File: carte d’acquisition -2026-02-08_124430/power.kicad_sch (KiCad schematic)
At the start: 59 parts, among them IC2 TPS259573DSGR, J10 Screw_Terminal_2_P5.00mm, U15 OKI-78SR-5_1.5-W36-C, U3 TPS55285, U4 MCP1799x-500xxTT, U5 INA3221, U9 TPS2116DRL

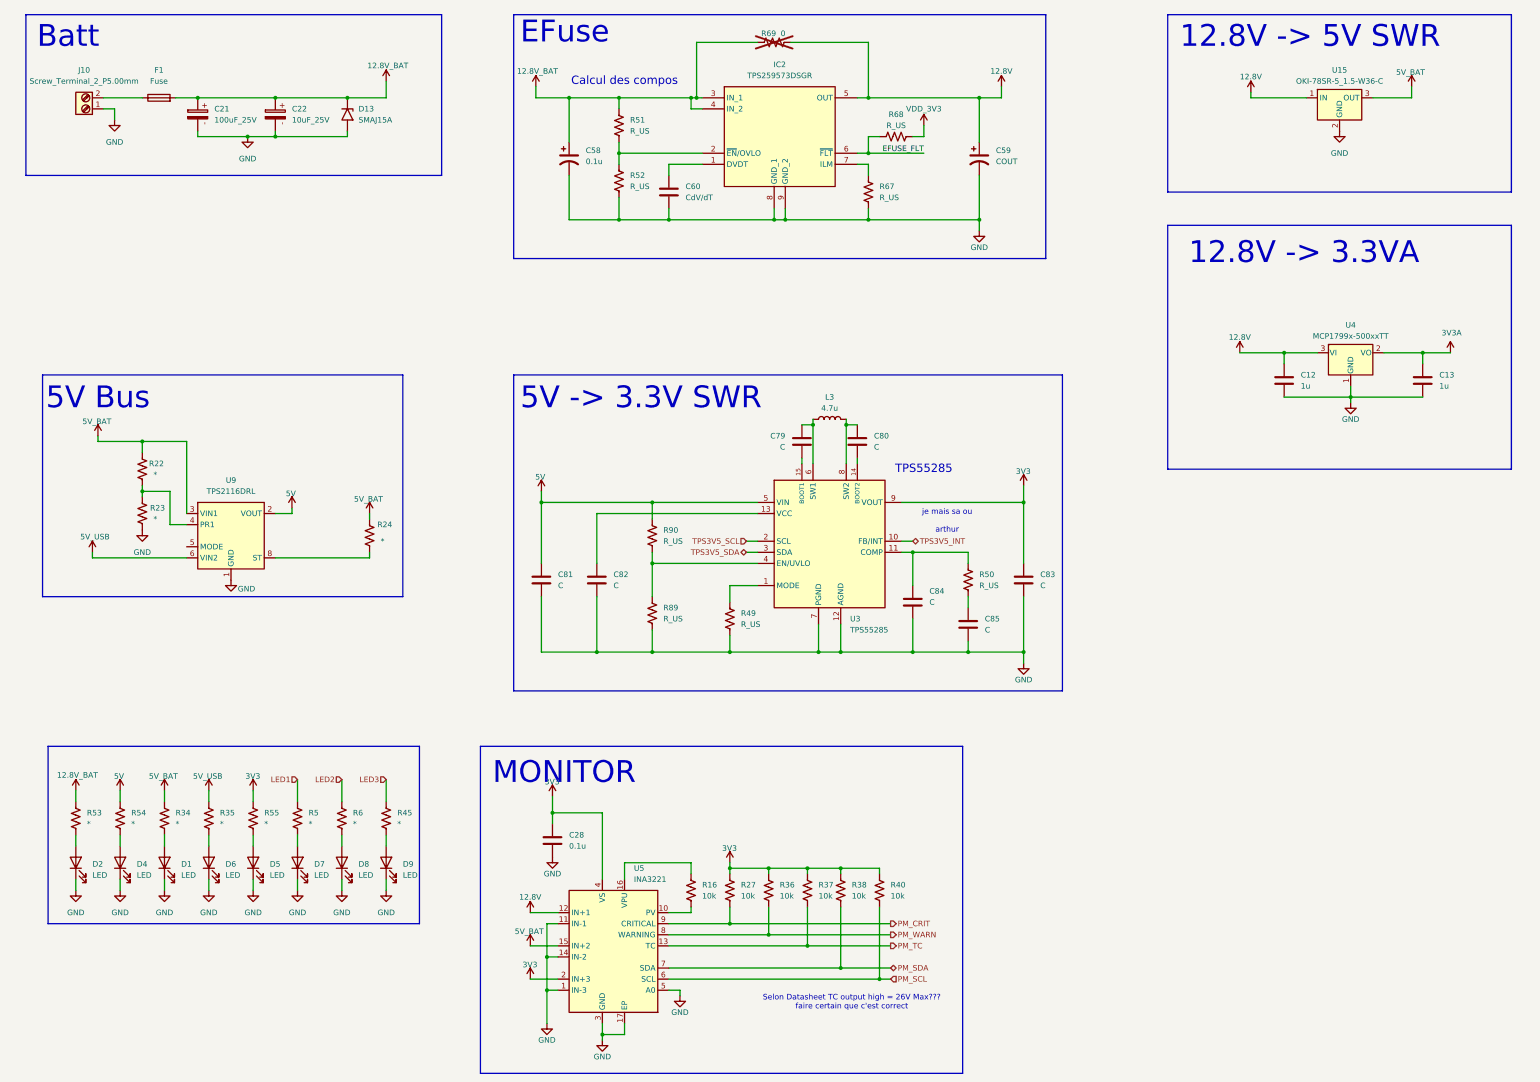
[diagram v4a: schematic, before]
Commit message: Ajout du 5VA et des borniers a vis pour loadcell
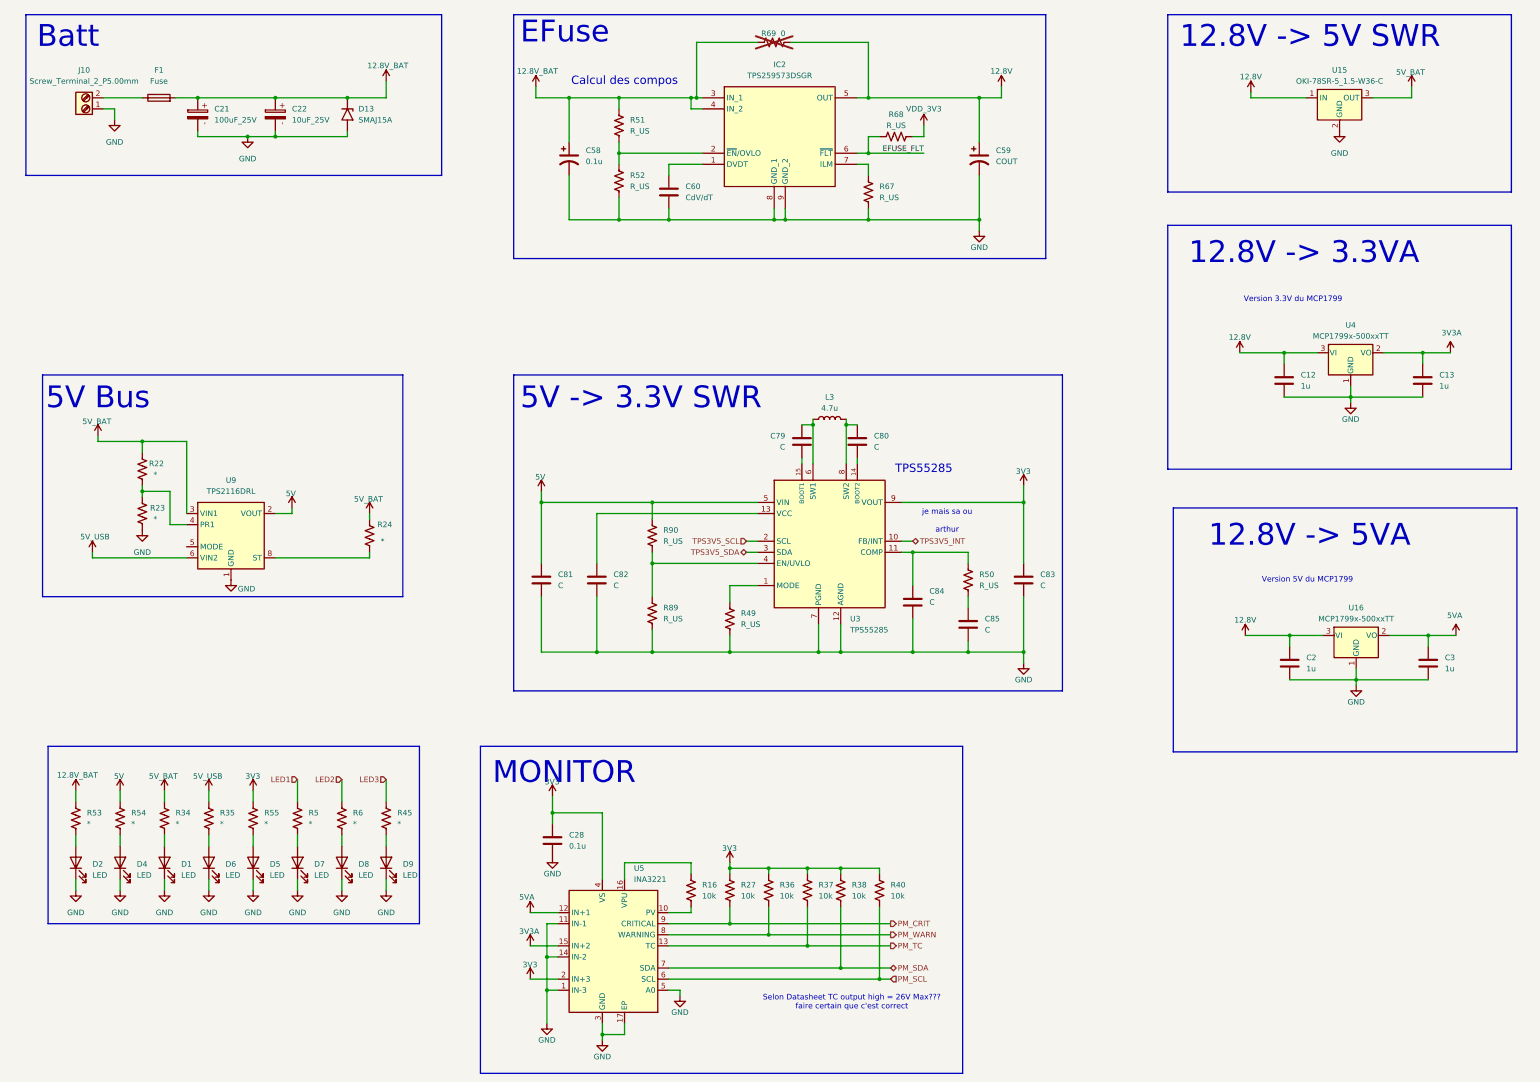
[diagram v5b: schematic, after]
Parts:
- added C2, C3: 1u, Capacitor_SMD:C_0603_1608Metric, symbol Device:C
- added U16: MCP1799x-500xxTT, Package_TO_SOT_SMD:SOT-23, symbol Regulator_Linear:MCP1799x-500xxTT
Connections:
- net 12.8V: now also C2.1, U16.3 (VI); no longer U5.12 (IN+1)
- net 3V3A: now also U5.15 (IN+2)
- net 5V_BAT: no longer U5.15 (IN+2)
- net GND: now also C2.2, C3.2, U16.1 (GND)
- new net 5VA: C3.1, U16.2 (VO), U5.12 (IN+1)
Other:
- note added: "12.8V -> 5VA"
- note added: "Version 3.3V du MCP1799"
- note added: "Version 5V du MCP1799"
